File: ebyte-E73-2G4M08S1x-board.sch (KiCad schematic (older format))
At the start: 39 parts, among them J1 USB_B_Micro, J2 USB_B_Micro, J3 BAT, J4 Conn_01x18_Male, J5 Conn_01x18_Male, J6 Conn_ARM_JTAG_SWD_10, J7 Conn_02x03_Odd_Even, Q1 PMV65XP, SW1 SW_Push, U1 MCP73831-2-OT, U2 LP5907MFX-3.3, U3 CH340E, U4 E73-2G4M08S1E, U5 L3GD20, Y1 Crystal

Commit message: Preliminary PCB layout
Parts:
- J1, J2: footprint Connector_USB:USB_Micro-AB_Molex_47590-0001 -> Connector_USB:USB_Micro-B_Amphenol_10103594-0001LF_Horizontal
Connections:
- net at C6.1, U4.11 (P0.00/XL1): now also Y1.2; no longer Y1.1
- net at C7.1, U4.13 (P0.01/XL2): now also Y1.1; no longer Y1.2
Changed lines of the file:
@@
 F 0 "J1" H 957 1867 50  0000 C CNN
 F 1 "USB_B_Micro" H 957 1776 50  0000 C CNN
-F 2 "Connector_USB:USB_Micro-AB_Molex_47590-0001" H 1050 1350 50  0001 C CNN
+F 2 "Connector_USB:USB_Micro-B_Amphenol_10103594-0001LF_Horizontal" H 1050 1350 50  0001 C CNN
 F 3 "~" H 1050 1350 50  0001 C CNN
 	1    900  1400
@@
 U 1 1 60519404
 P 4450 1150
-F 0 "Y1" V 4404 1281 50  0000 L CNN
-F 1 "Crystal" V 4495 1281 50  0000 L CNN
+F 0 "Y1" V 4100 1100 50  0000 L CNN
+F 1 "Crystal" V 4200 1050 50  0000 L CNN
 F 2 "Crystal:Crystal_SMD_MicroCrystal_MS3V-T1R" H 4450 1150 50  0001 C CNN
 F 3 "~" H 4450 1150 50  0001 C CNN
 	1    4450 1150
-	0    1    1    0
+	0    -1   -1   0
 $EndComp
 $Comp
@@
 F 0 "J2" H 957 3217 50  0000 C CNN
 F 1 "USB_B_Micro" H 957 3126 50  0000 C CNN
-F 2 "Connector_USB:USB_Micro-AB_Molex_47590-0001" H 1050 2700 50  0001 C CNN
+F 2 "Connector_USB:USB_Micro-B_Amphenol_10103594-0001LF_Horizontal" H 1050 2700 50  0001 C CNN
 F 3 "~" H 1050 2700 50  0001 C CNN
 	1    900  2750

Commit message: Update sch, pcb, bom
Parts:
- removed TP1: TestPoint, TestPoint:TestPoint_Pad_1.0x1.0mm, symbol Connector:TestPoint
- added D6, D8: LED, LED_SMD:LED_0603_1608Metric, symbol Device:LED
- added R5: 10k, Resistor_SMD:R_0603_1608Metric, symbol Device:R
- added R7, R8: 470R, Resistor_SMD:R_0603_1608Metric, symbol Device:R
- added SW2: PTS810, Button_Switch_SMD:SW_SPST_PTS810, symbol Switch:SW_Push
- C3: value 0.1 -> 100n
- R4: value R -> 470R
- SW1: value SW_Push -> PTS810
- Y1: value Crystal -> 32768
- renumbered C8 to C6, C6 to C7, C7 to C8, D6 to D5, D5 to D7, R5 to R6, TP3 to TP1, U5 to U4, U4 to U5
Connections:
- net GND: now also R8.1, SW2.2
- net P0.04: now also D7.4 (DIN)
- net P0.15: now also R7.2; no longer D7.4 (DIN)
- net RST: now also R5.1, SW2.1
- net VDD: now also D6.2 (A), R5.2
- net at C7.1, U5.11 (P0.00/XL1): now also Y1.1; no longer Y1.2
- net at C8.1, U5.13 (P0.01/XL2): now also Y1.2; no longer Y1.1
- net at U3.6 (TNOW): now also D8.2 (A)
- new net: D6.1 (K), R7.1
- new net: D8.1 (K), R8.2
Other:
- note removed: "TODO:\n- change button to top push: I don't have such\n- add external pinout\n- connect external pins\n- add accelerometer: L3GD20 (obsolete)\n"
- moved on the sheet: D5, D7, R6, SW1, Y1

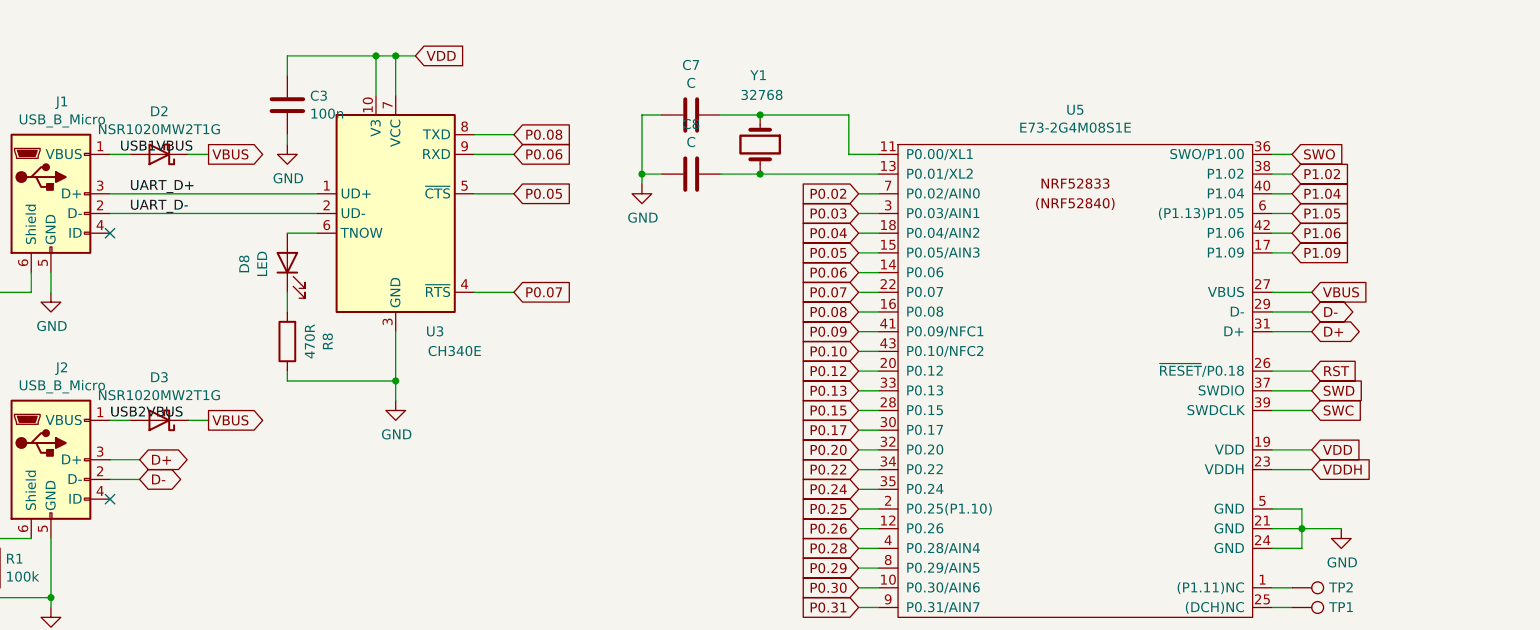
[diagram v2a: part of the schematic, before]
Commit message: Improve silk
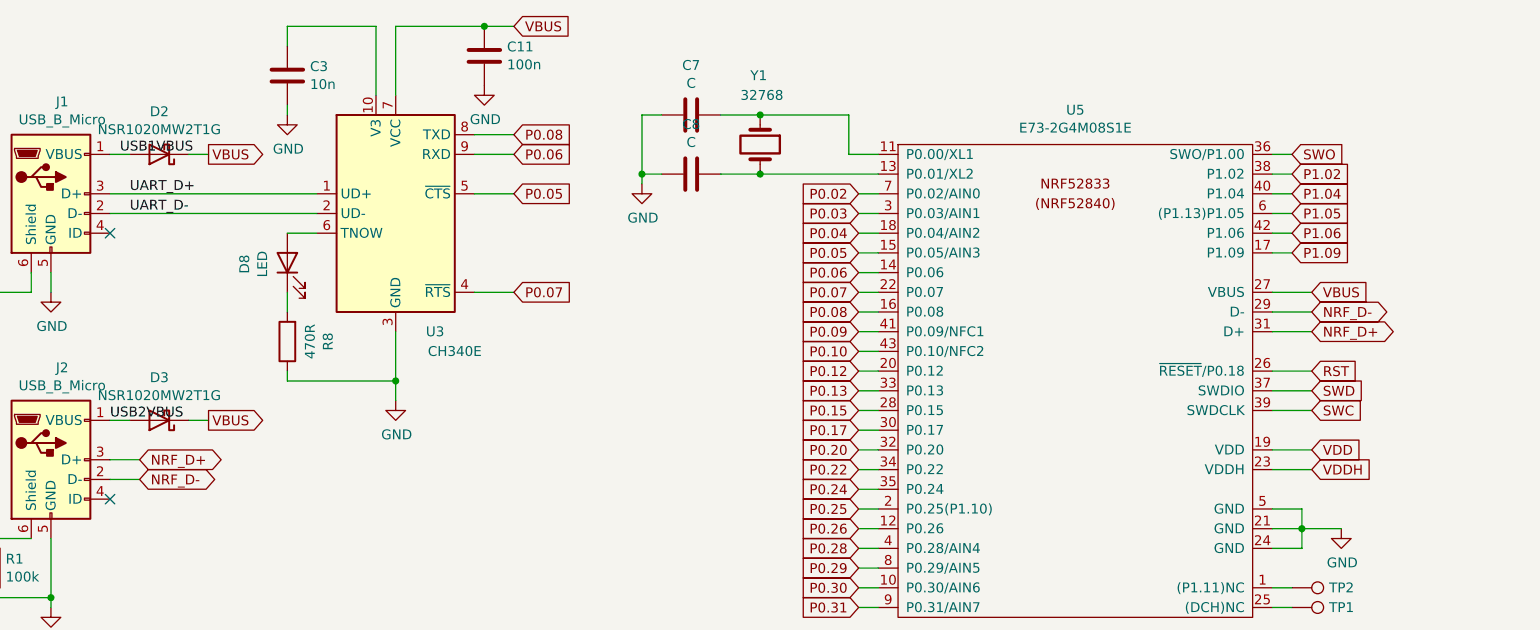
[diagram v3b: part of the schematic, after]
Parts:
- added C11: 100n, Capacitor_SMD:C_0603_1608Metric, symbol Device:C
- C3: value 100n -> 10n
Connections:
- net GND: now also C11.1
- net VBUS: now also U3.7 (VCC), C11.2
- net VDD: no longer C3.2, U3.10 (V3), U3.7 (VCC)
- net D+ renamed NRF_D+
- net D- renamed NRF_D-
- new net: C3.2, U3.10 (V3)
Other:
- moved on the sheet: C3
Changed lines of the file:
@@
 VBUS
 Text GLabel 7300 2000 2    50   BiDi ~ 0
-D-
+NRF_D-
 Text GLabel 7300 2100 2    50   BiDi ~ 0
-D+
+NRF_D+
 $Comp
 L power:GND #PWR012
@@
 	2250 1600 2100 1600
 Wire Wire Line
-	2550 900  2550 700
-Wire Wire Line
-	2550 700  2650 700
-Wire Wire Line
-	2650 700  2650 900
-Text GLabel 2750 700  2    50   Input ~ 0
-VDD
-Wire Wire Line
-	2750 700  2650 700
-Connection ~ 2650 700
+	2550 900  2550 550
+Text GLabel 3250 550  2    50   Input ~ 0
+VBUS
 $Comp
 L Device:C C3
 U 1 1 6059A17F
-P 2100 950
-F 0 "C3" H 1985 904 50  0000 R CNN
-F 1 "100n" H 1985 995 50  0000 R CNN
-F 2 "Capacitor_SMD:C_0603_1608Metric" H 2138 800 50  0001 C CNN
-F 3 "~" H 2100 950 50  0001 C CNN
-	1    2100 950
+P 2100 800
+F 0 "C3" H 1985 754 50  0000 R CNN
+F 1 "10n" H 1985 845 50  0000 R CNN
+F 2 "Capacitor_SMD:C_0603_1608Metric" H 2138 650 50  0001 C CNN
+F 3 "~" H 2100 800 50  0001 C CNN
+	1    2100 800
 	-1   0    0    1
 $EndComp
 Wire Wire Line
-	2550 700  2100 700
-Wire Wire Line
-	2100 700  2100 800
-Connection ~ 2550 700
+	2550 550  2100 550
+Wire Wire Line
+	2100 550  2100 650
 $Comp
 L power:GND #PWR06
 U 1 1 605A0222
-P 2100 1150
-F 0 "#PWR06" H 2100 900 50  0001 C CNN
-F 1 "GND" H 2105 977 50  0000 C CNN
-F 2 "" H 2100 1150 50  0001 C CNN
-F 3 "" H 2100 1150 50  0001 C CNN
-	1    2100 1150
-	1    0    0    -1
-$EndComp
-Wire Wire Line
-	2100 1100 2100 1150
+P 2100 1000
+F 0 "#PWR06" H 2100 750 50  0001 C CNN
+F 1 "GND" H 2105 827 50  0000 C CNN
+F 2 "" H 2100 1000 50  0001 C CNN
+F 3 "" H 2100 1000 50  0001 C CNN
+	1    2100 1000
+	1    0    0    -1
+$EndComp
+Wire Wire Line
+	2100 950  2100 1000
 Wire Wire Line
 	2650 2450 2650 2350
@@
 VBUS
 Text GLabel 1350 2850 2    50   BiDi ~ 0
-D-
+NRF_D-
 Text GLabel 1350 2750 2    50   BiDi ~ 0
-D+
+NRF_D+
 Wire Wire Line
 	1350 2750 1200 2750
@@
 Wire Wire Line
 	2650 2350 2650 2100
+Wire Wire Line
+	2650 900  2650 550
+Wire Wire Line
+	2650 550  3100 550
+$Comp
+L Device:C C11
+U 1 1 60B742F4
+P 3100 700
+F 0 "C11" H 2985 654 50  0000 R CNN
+F 1 "100n" H 2985 745 50  0000 R CNN
+F 2 "Capacitor_SMD:C_0603_1608Metric" H 3138 550 50  0001 C CNN
+F 3 "~" H 3100 700 50  0001 C CNN
+	1    3100 700
+	-1   0    0    1
+$EndComp
+Connection ~ 3100 550
+Wire Wire Line
+	3100 550  3250 550
+$Comp
+L power:GND #PWR013
+U 1 1 60BDB32C
+P 3100 850
+F 0 "#PWR013" H 3100 600 50  0001 C CNN
+F 1 "GND" H 3105 677 50  0000 C CNN
+F 2 "" H 3100 850 50  0001 C CNN
+F 3 "" H 3100 850 50  0001 C CNN
+	1    3100 850
+	1    0    0    -1
+$EndComp
 $EndSCHEMATC
